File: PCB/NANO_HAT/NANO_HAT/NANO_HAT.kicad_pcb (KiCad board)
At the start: 2 copper layers, 18 parts, among them J1 Conn_01x03_Male, J2 Conn_01x02_Male, J3 Conn_01x02_Male, J4 Conn_01x04_Male, J5 Conn_01x02_Male, J6 Conn_01x02_Male, J7 Conn_01x04_Male, U1 DMN4026SSD

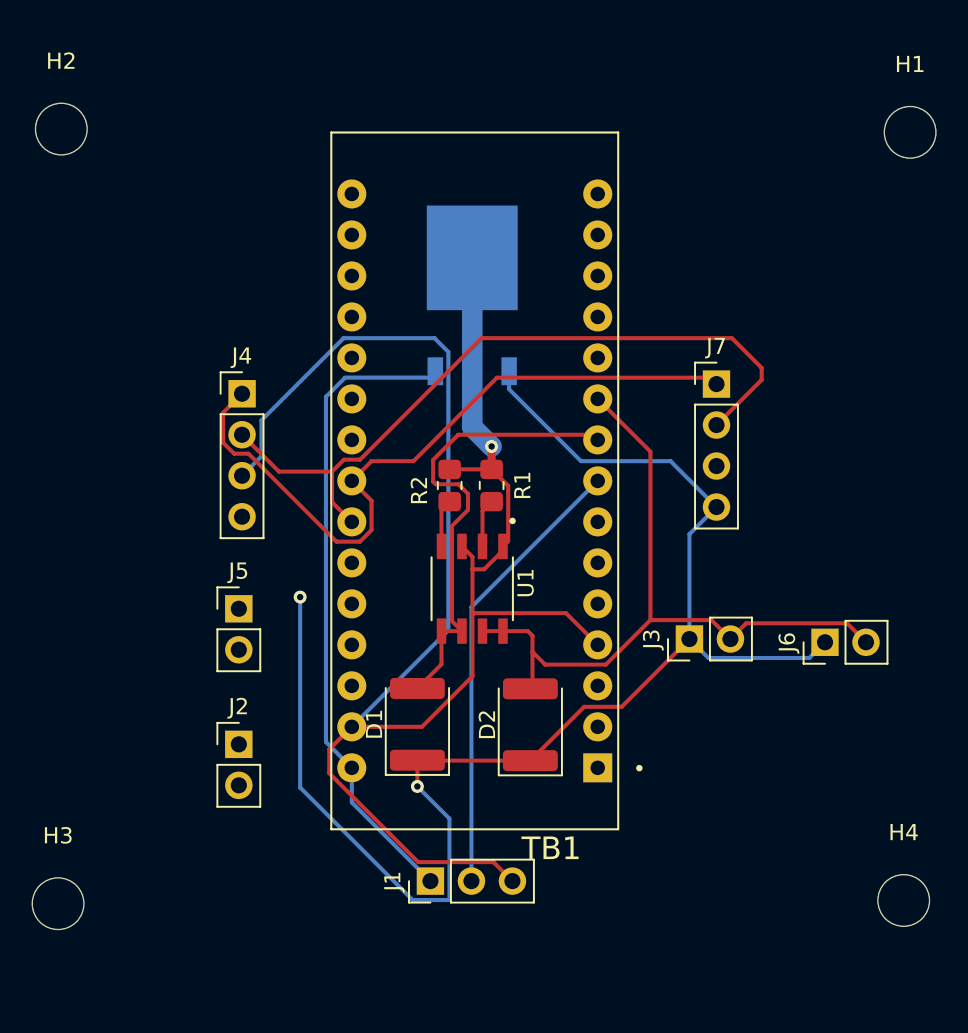
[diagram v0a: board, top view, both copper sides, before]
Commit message: updated NANO_HAT
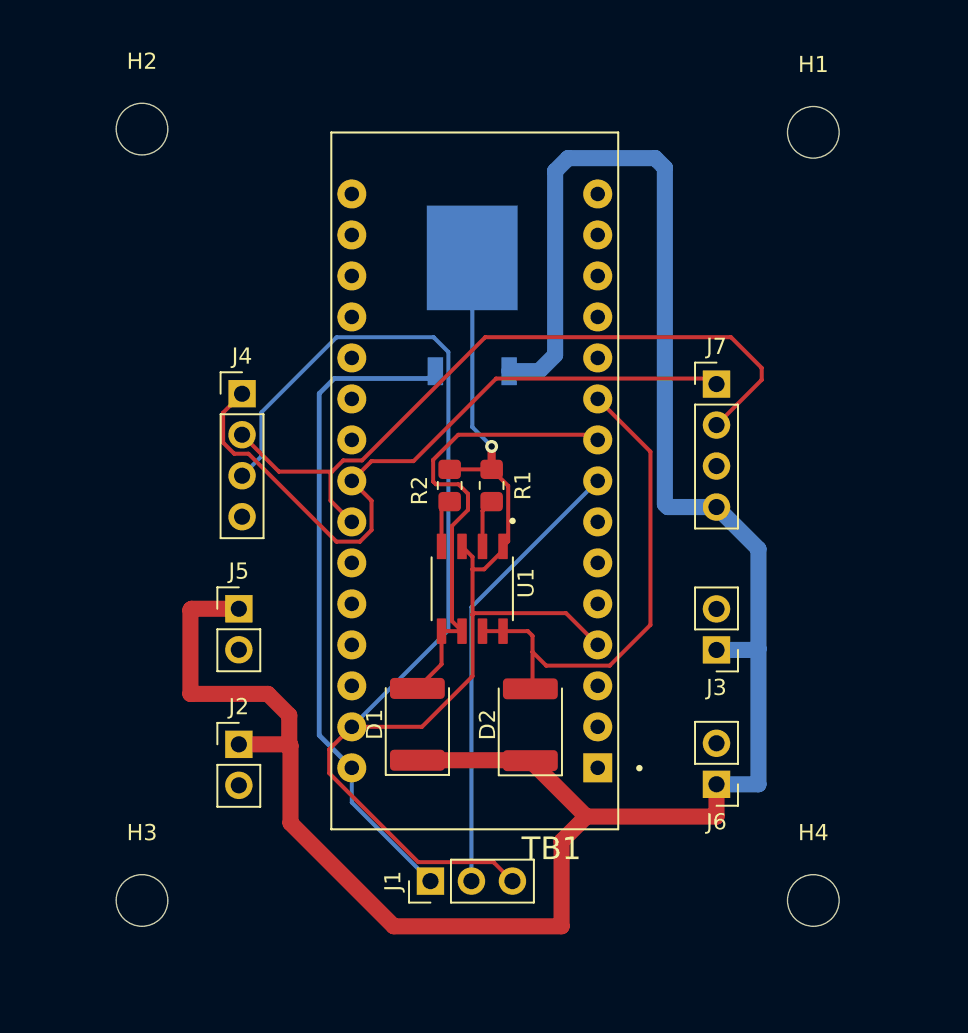
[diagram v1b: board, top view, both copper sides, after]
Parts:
- moved J6 11.1 mm to (177.2, 104.6), turned to 180 degrees
- moved H1 6.00 mm to (183.2, 64.2)
- moved H4 5.60 mm to (183.2, 111.8)
- moved H3 5.20 mm to (141.6, 111.8)
- moved H2 5.00 mm to (141.6, 64.0)
- moved J3 1.81 mm to (177.2, 96.3), turned to 180 degrees
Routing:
- net VCC: track 88.6 -> 143.3 mm, vias 2 -> 0
- net /SOL2: track 45.1 -> 30.6 mm
- net /5V: track 40.1 -> 40.8 mm

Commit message: Updated
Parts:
- added G***: LOGO, .pretty:eppl_logo, F.Cu at (140.7, 87.5)
- D1, D2, R1, R2, U1: moved to B.Cu
- J1: value Conn_01x03_Male -> LED
- J2, J5: value Conn_01x02_Male -> SOL1
- J3, J6: value Conn_01x02_Male -> SOL2
- moved D1 7.00 mm to (165.7, 100.9)
- moved D2 7.00 mm to (158.7, 100.9)
- moved R2 3.00 mm to (163.7, 86.1)
- moved R1 2.20 mm to (161.1, 86.1)
- moved U1 0.20 mm to (162.3, 92.5)
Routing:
- net GND: track 111.5 -> 49.8 mm
- net /SOL2: track 30.6 -> 51.0 mm
- net /SOL1: track 29.4 -> 49.1 mm, vias 0 -> 1
- net unconnected-(TB1-Pad28): track 0.00 -> 15.2 mm
- net /LED: track 28.0 -> 33.3 mm
- net /5V: track 40.8 -> 36.4 mm
- net VCC: track 143.3 -> 141.8 mm
- added copper zone on F.Cu, net GND
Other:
- board outline added: 51.6 x 59.1 mm
- board text added: "12V"
- board text added: "5V"
- board text added: "GND"
- board text added: "LED"
- board text added: "SCL"
- board text added: "SDA"

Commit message: Updated (Gerber)
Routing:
- net GND: track 49.8 -> 54.8 mm, vias 1 -> 2
- net /5V: track 36.4 -> 35.8 mm
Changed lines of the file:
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@@
       (outputformat 1)
       (mirror false)
-      (drillshape 1)
+      (drillshape 0)
       (scaleselection 1)
-      (outputdirectory "")
+      (outputdirectory "Gerber")
     )
   )
@@
     (fp_line (start 1 0.625) (end 1 -0.625) (layer "B.Fab") (width 0.1))
     (fp_line (start -1 0.625) (end 1 0.625) (layer "B.Fab") (width 0.1))
-    (pad "1" smd roundrect (at -1 0 270) (size 1.2 1.4) (layers "B.Cu" "B.Paste" "B.Mask") (roundrect_rratio 0.208333)
+    (pad "1" smd roundrect (at -1 0 270) (size 1.2 1.4) (layers "B.Cu" "B.Paste" "B.Mask") (roundrect_rratio 0.2083333333)
       (net 5 "GND") (pintype "passive"))
-    (pad "2" smd roundrect (at 1 0 270) (size 1.2 1.4) (layers "B.Cu" "B.Paste" "B.Mask") (roundrect_rratio 0.208333)
+    (pad "2" smd roundrect (at 1 0 270) (size 1.2 1.4) (layers "B.Cu" "B.Paste" "B.Mask") (roundrect_rratio 0.2083333333)
       (net 8 "/Gate 1") (pintype "passive"))
     (model "${KICAD6_3DMODEL_DIR}/Resistor_SMD.3dshapes/R_0805_2012Metric.wrl"
@@
     (fp_line (start -2.25 0.8) (end -2.25 -1.6) (layer "B.Fab") (width 0.1))
     (fp_line (start -1.45 1.6) (end -2.25 0.8) (layer "B.Fab") (width 0.1))
-    (pad "1" smd roundrect (at -2.225 0 90) (size 1.3 3.4) (layers "B.Cu" "B.Paste" "B.Mask") (roundrect_rratio 0.192308)
+    (pad "1" smd roundrect (at -2.225 0 90) (size 1.3 3.4) (layers "B.Cu" "B.Paste" "B.Mask") (roundrect_rratio 0.1923076923)
       (net 1 "VCC") (pinfunction "K") (pintype "passive"))
-    (pad "2" smd roundrect (at 2.225 0 90) (size 1.3 3.4) (layers "B.Cu" "B.Paste" "B.Mask") (roundrect_rratio 0.192308)
+    (pad "2" smd roundrect (at 2.225 0 90) (size 1.3 3.4) (layers "B.Cu" "B.Paste" "B.Mask") (roundrect_rratio 0.1923076923)
       (net 3 "/SOL2") (pinfunction "A") (pintype "passive"))
     (model "${KICAD6_3DMODEL_DIR}/Diode_SMD.3dshapes/D_1812_4532Metric.wrl"
@@
     (fp_line (start 1 -0.625) (end -1 -0.625) (layer "B.Fab") (width 0.1))
     (fp_line (start -1 0.625) (end 1 0.625) (layer "B.Fab") (width 0.1))
-    (pad "1" smd roundrect (at -1 0 270) (size 1.2 1.4) (layers "B.Cu" "B.Paste" "B.Mask") (roundrect_rratio 0.208333)
+    (pad "1" smd roundrect (at -1 0 270) (size 1.2 1.4) (layers "B.Cu" "B.Paste" "B.Mask") (roundrect_rratio 0.2083333333)
       (net 5 "GND") (pintype "passive"))
-    (pad "2" smd roundrect (at 1 0 270) (size 1.2 1.4) (layers "B.Cu" "B.Paste" "B.Mask") (roundrect_rratio 0.208333)
+    (pad "2" smd roundrect (at 1 0 270) (size 1.2 1.4) (layers "B.Cu" "B.Paste" "B.Mask") (roundrect_rratio 0.2083333333)
       (net 9 "/Gate 2") (pintype "passive"))
     (model "${KICAD6_3DMODEL_DIR}/Resistor_SMD.3dshapes/R_0805_2012Metric.wrl"
@@
     (fp_line (start -1.45 1.6) (end -2.25 0.8) (layer "B.Fab") (width 0.1))
     (fp_line (start 2.25 -1.6) (end 2.25 1.6) (layer "B.Fab") (width 0.1))
-    (pad "1" smd roundrect (at -2.225 0 90) (size 1.3 3.4) (layers "B.Cu" "B.Paste" "B.Mask") (roundrect_rratio 0.192308)
+    (pad "1" smd roundrect (at -2.225 0 90) (size 1.3 3.4) (layers "B.Cu" "B.Paste" "B.Mask") (roundrect_rratio 0.1923076923)
       (net 1 "VCC") (pinfunction "K") (pintype "passive"))
-    (pad "2" smd roundrect (at 2.225 0 90) (size 1.3 3.4) (layers "B.Cu" "B.Paste" "B.Mask") (roundrect_rratio 0.192308)
+    (pad "2" smd roundrect (at 2.225 0 90) (size 1.3 3.4) (layers "B.Cu" "B.Paste" "B.Mask") (roundrect_rratio 0.1923076923)
       (net 2 "/SOL1") (pinfunction "A") (pintype "passive"))
     (model "${KICAD6_3DMODEL_DIR}/Diode_SMD.3dshapes/D_1812_4532Metric.wrl"
@@
   (segment (start 163.380489 109.425489) (end 158.713768 109.425489) (width 0.25) (layer "F.Cu") (net 5))
   (segment (start 153.2 103.911721) (end 153.2 102.44) (width 0.25) (layer "F.Cu") (net 5))
+  (via (at 168.4 84.55) (size 0.8) (drill 0.4) (layers "F.Cu" "B.Cu") (net 5))
   (via (at 162 67) (size 0.8) (drill 0.4) (layers "F.Cu" "B.Cu") (net 5))
   (segment (start 162.9 90.8) (end 162.9 89.86) (width 0.25) (layer "B.Cu") (net 5))
   (segment (start 162.065 71.9825) (end 162.065 84.085) (width 0.25) (layer "B.Cu") (net 5))
   (segment (start 161.065 85.085) (end 161 85.15) (width 0.254) (layer "B.Cu") (net 5))
+  (segment (start 163.665 85.085) (end 167.865 85.085) (width 0.25) (layer "B.Cu") (net 5))
   (segment (start 159.5 85.65) (end 159.5 89) (width 0.254) (layer "B.Cu") (net 5))
   (segment (start 160.36 90.76) (end 160.85 91.25) (width 0.25) (layer "B.Cu") (net 5))
@@
   (segment (start 162.065 71.9825) (end 162.065 67.065) (width 0.254) (layer "B.Cu") (net 5))
   (segment (start 159.5 89) (end 160.36 89.86) (width 0.254) (layer "B.Cu") (net 5))
+  (segment (start 167.865 85.085) (end 168.4 84.55) (width 0.25) (layer "B.Cu") (net 5))
   (segment (start 162.065 84.085) (end 161.065 85.085) (width 0.25) (layer "B.Cu") (net 5))
   (segment (start 162.065 67.065) (end 162 67) (width 0.254) (layer "B.Cu") (net 5))
@@
   (segment (start 164.17 87.59) (end 164.17 89.86) (width 0.25) (layer "B.Cu") (net 9))
   (segment (start 169.84 98.5) (end 154.6 98.5) (width 0.254) (layer "F.Cu") (net 12))
-  (segment (start 159.78 79.0025) (end 159.377989 79.404511) (width 0.25) (layer "B.Cu") (net 31))
   (segment (start 154.6 105.725) (end 159.475 110.6) (width 0.25) (layer "B.Cu") (net 31))
-  (segment (start 156.1 82.6825) (end 159.78 79.0025) (width 0.254) (layer "B.Cu") (net 31))
   (segment (start 154.6 103.58) (end 156.1 102.08) (width 0.254) (layer "B.Cu") (net 31))
   (segment (start 156.1 102.08) (end 156.1 82.6825) (width 0.254) (layer "B.Cu") (net 31))
-  (segment (start 159.377989 79.404511) (end 159.352989 79.429511) (width 0.3) (layer "B.Cu") (net 31))
   (segment (start 154.6 103.58) (end 154.6 105.725) (width 0.25) (layer "B.Cu") (net 31))
+  (segment (start 159.78 79.0025) (end 156.1 82.6825) (width 0.25) (layer "B.Cu") (net 31))
   (zone (net 5) (net_name "GND") (layer "F.Cu") (hatch edge 0.508)
     (connect_pads (clearance 0.508))
